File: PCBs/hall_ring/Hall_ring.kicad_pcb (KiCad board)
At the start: 2 copper layers, 38.5 x 37.5 mm, 19 parts, among them J1 Conn_02x05_Odd_Even, J2 Conn_01x03_Female, U1 DRV5053_LPG, U2 DRV5053_LPG, U3 DRV5053_LPG, U4 DRV5053_LPG, U5 DRV5053_LPG, U6 DRV5053_LPG, U7 DRV5053_LPG

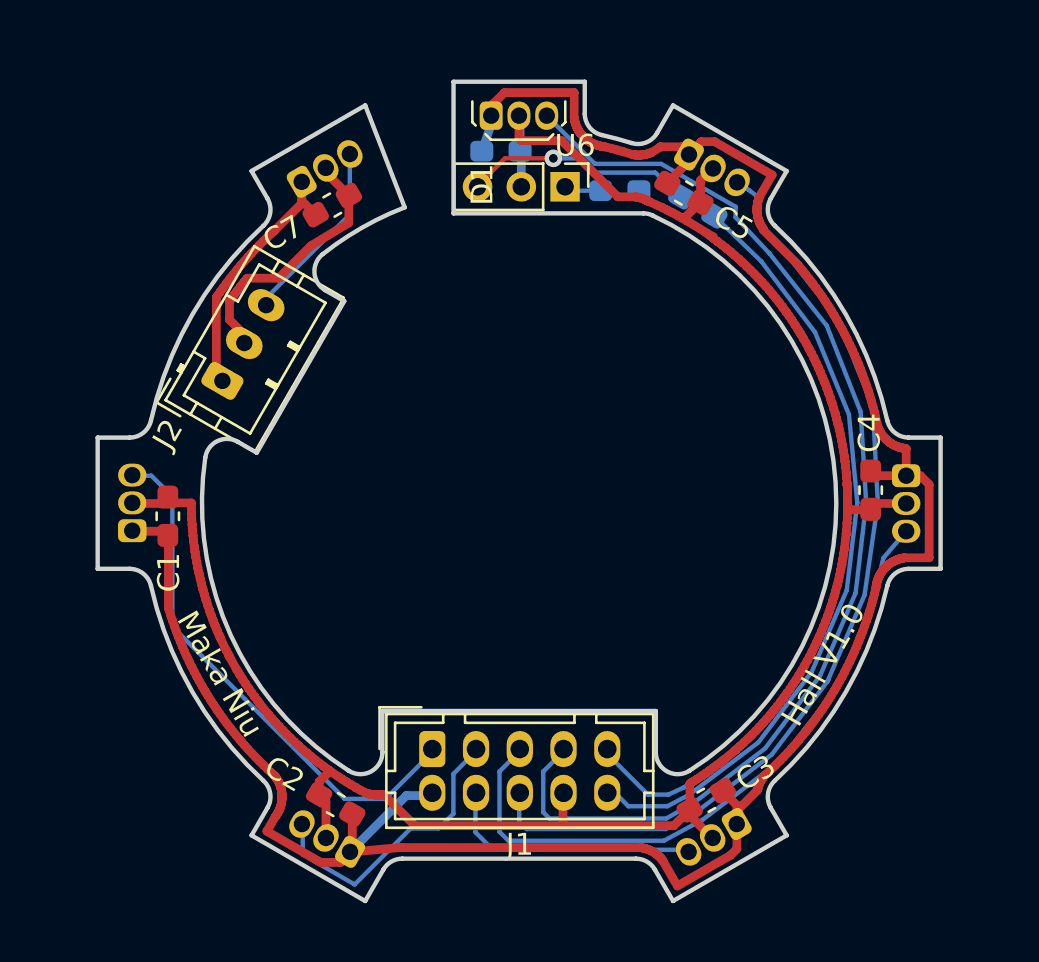
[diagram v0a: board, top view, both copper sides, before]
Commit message: updates to battery managemennt wayfinder boards, and makaniu hall sensor ring and BMS
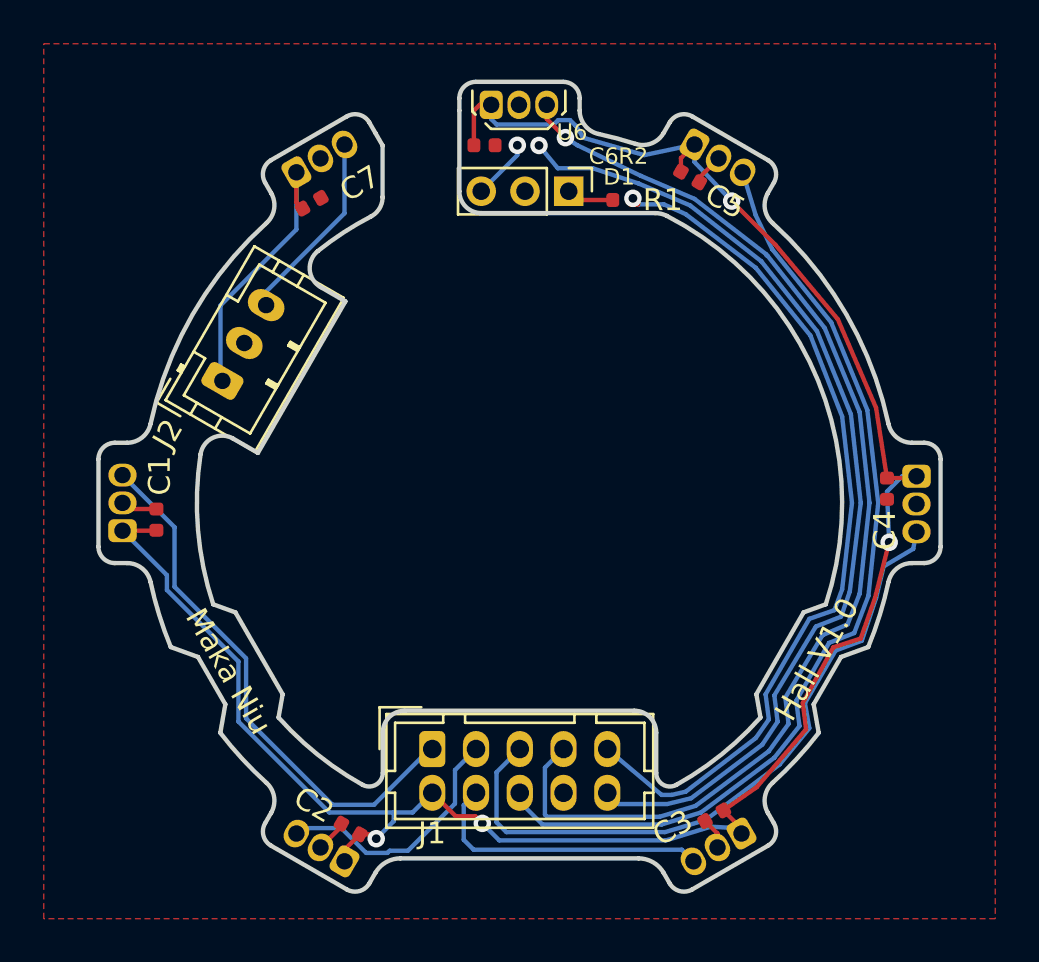
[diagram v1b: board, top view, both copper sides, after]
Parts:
- C1, C2, C3, C4, C5, C7: footprint Capacitor_SMD:C_0603_1608Metric_Pad1.05x0.95mm_HandSolder -> Capacitor_SMD:C_0402_1005Metric
- C6: footprint Capacitor_SMD:C_0603_1608Metric_Pad1.05x0.95mm_HandSolder -> Capacitor_SMD:C_0402_1005Metric; moved to F.Cu
- R1, R2: footprint Resistor_SMD:R_0603_1608Metric_Pad1.05x0.95mm_HandSolder -> Resistor_SMD:R_0402_1005Metric; moved to F.Cu
- moved R2 8.24 mm to (127.4, 113.2), turned to 180 degrees
- moved C2 1.31 mm to (119.3, 144.4)
- moved C7 0.94 mm to (117.5, 115.8)
- moved C6 0.80 mm to (125.4, 113.2)
- moved C3 0.79 mm to (135.9, 143.8)
- moved C5 0.79 mm to (134.8, 114.6)
- moved C4 0.75 mm to (143.8, 128.9)
- moved C1 0.54 mm to (110.4, 130.3)
- moved U5 0.52 mm to (135.0, 113.2)
- moved U2 0.50 mm to (119.0, 145.9)
- moved U7 0.50 mm to (116.8, 114.4)
- moved U6 0.50 mm to (125.7, 111.3)
- moved U3 0.49 mm to (137.1, 144.7)
- moved U4 0.47 mm to (145.2, 128.3)
- moved R1 0.46 mm to (131.8, 115.7)
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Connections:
- C7 pad 2: Net-(C7-Pad2) -> GND
- J2 pad 2: Net-(C7-Pad2) -> GND
- U7 pad 2: Net-(C7-Pad2) -> GND
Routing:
- net GND: track 93.4 -> 5.92 mm
- net Net-(C7-Pad2): track 12.2 -> 0.00 mm
- net VCC: track 109.2 -> 97.9 mm, vias 0 -> 4
- net Net-(J1-Pad10): track 35.4 -> 45.0 mm, vias 0 -> 1
- net Net-(D1-Pad3): track 10.5 -> 2.78 mm
- net /hall_3: track 11.6 -> 13.3 mm
- net /hall_2: track 13.2 -> 11.7 mm
- net Net-(D1-Pad1): track 1.88 -> 3.03 mm
- net Net-(J1-Pad9): track 38.3 -> 39.4 mm, vias 0 -> 1
- net Net-(C7-Pad1): track 11.8 -> 12.8 mm
- net /hall_4: track 30.3 -> 31.1 mm
- net /hall_button: track 52.1 -> 52.8 mm, vias 0 -> 1
- net /hall_5: track 44.0 -> 43.5 mm
- net /hall_1: track 24.1 -> 24.7 mm
- added copper zone on F.Cu, net GND
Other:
- board size 38.5 x 37.5 mm -> 38.5 x 37 mm
- net class Default: clearance 0.2 -> 0.15
- net class Power removed
- rule trace_clearance: 0.2 -> 0.15
